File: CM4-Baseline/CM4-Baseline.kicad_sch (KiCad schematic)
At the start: 0 parts

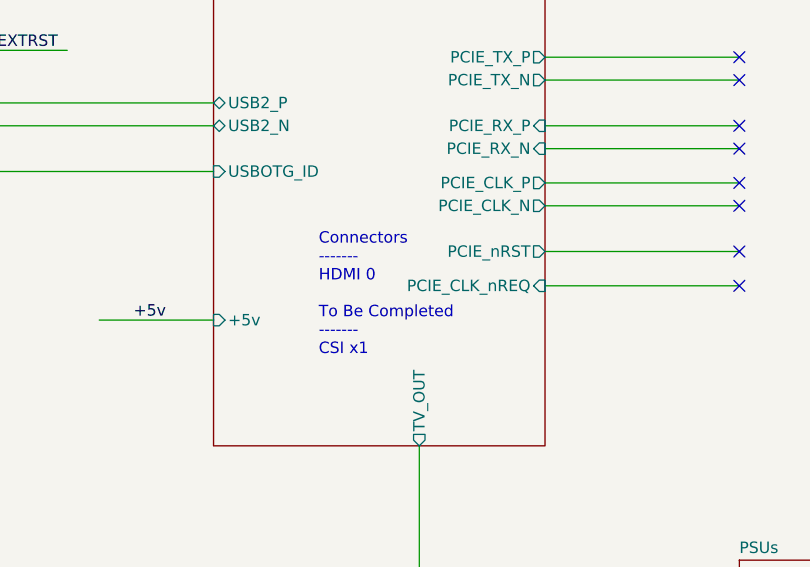
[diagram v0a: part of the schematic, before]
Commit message: Added CSI connector and associated library
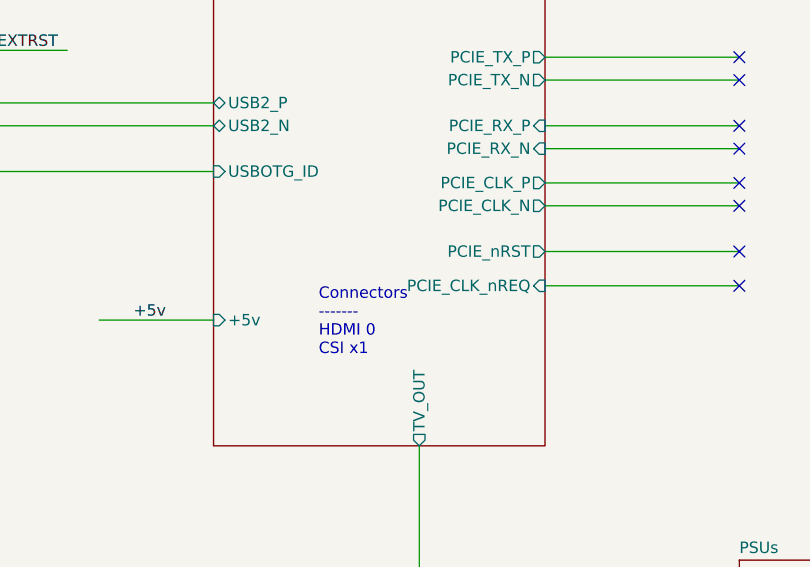
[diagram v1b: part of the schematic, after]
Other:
- note added: "Connectors ------- HDMI 0 CSI x1"
- note removed: "Connectors ------- HDMI 0 To Be Completed ------- CSI x1"
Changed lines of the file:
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@@
 		)
 	)
-	(text "Connectors\n-------\nHDMI 0\n\nTo Be Completed\n-------\nCSI x1\n"
+	(text "Connectors\n-------\nHDMI 0\nCSI x1\n"
 		(exclude_from_sim no)
 		(at 125.984 80.264 0)
